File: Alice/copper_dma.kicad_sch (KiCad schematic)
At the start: 36 parts

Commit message: Copper DMA done
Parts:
- added AND_134, AND_136, AND_137, AND_138, AND_139, AND_140, AND_141, AND_142, AND_143, AND_39: AND2, symbol NMOS:AND2
- added AND_135: AND3, symbol NMOS:AND3
- added COP1_FF1, COP2_FF1, COP3_FF1: DFFR, symbol NMOS:DFFR
- added COP3D_FF1: DFFN, symbol NMOS:DFFN
- added NAND_9: NAND2, symbol NMOS:NAND2
- added NOR_34, NOR_35, NOR_37: NOR2, symbol NMOS:NOR2
- added NOR_36: NOR6, symbol NMOS:NOR6
- added NOR_38: NOR4, symbol NMOS:NOR4
- added NOT_36, NOT_37: NOT, symbol NMOS:NOT
- added OR_49, OR_51, OR_52: OR2, symbol NMOS:OR2
- added OR_50: OR4, symbol NMOS:OR4
- added Q898, Q899, Q900, Q901, Q902, Q903, Q904, Q905, Q906, Q907: NOT_OC, symbol NMOS:NOT_OC
- added SKIP_SR1: SR, symbol NMOS:SR
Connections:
- net COPEN: now also AND_128.3, AND_39.3; no longer AND_128.4
- net COPRES: now also COP1_FF1.6 (R), COP2_FF1.6 (R), COP3_FF1.6 (R), OR_52.2
- net COPSTART: now also AND_134.3, OR_49.3, OR_50.2
- net CPCE: now also AND_134.2, AND_137.3, AND_138.3, AND_139.3, AND_140.3, AND_141.3, AND_142.3
- net EQGT: now also AND_135.4, NOR_34.3
- net GND: now also NOR_36.3
- net HCTR1: now also AND_128.4, NOR_38.4, NOT_36.2; no longer AND_128.3
- net PHI1: now also COP1_FF1.4 (C1), COP2_FF1.4 (C1), COP3D_FF1.4 (C1), COP3_FF1.4 (C1), SKIP_SR1.4 (C1)
- net PHI2: now also AND_137.2, COP3D_FF1.5 (C2)
- net UCI1: now also AND_139.1, Q898.2, Q900.2, Q902.2, Q904.2, Q906.2
- net UCI2: now also AND_142.1, Q899.2, Q901.2, Q903.2, Q905.2, Q907.2
- net VALIDMOVE: now also AND_136.2, NOT_37.2
- net MOVE: now reaches AND_133.2, CIR1_LD0.2 (~{Q})
- net MOVE: now also NOR_36.4
- net CBR2: now reaches COPJMP_SR2.1 (Q), OR_47.2
- net CBR2: now also AND_141.2
- net at COPJMP_SR2.6 (R): now also COPJMP_SR1.6 (R), AND_134.1
- net CBR1: now reaches COPJMP_SR1.1 (Q), OR_47.3
- net CBR1: now also AND_140.2
- net SKIP_INS renamed SKIPINS
- net SKIPINS: now also AND_135.3, NOR_34.2
- new net: NOR_34.1, NOR_36.2
- new net: AND_39.2, NOT_36.1
- new net: COP2_FF1.3 (D), NOR_37.1
- new net: NOR_35.1, NOR_37.3
- new net: OR_52.1, SKIP_SR1.6 (R)
- new net: NOR_38.5, NOT_37.1
- new net: COP3D_FF1.2 (~{Q}), NAND_9.2
- new net: COP1_FF1.3 (D), OR_49.1
- new net: NAND_9.1, NOR_38.3
- new net CIPRQ: AND_139.2, OR_51.1
- new net COP1: AND_135.2, COP1_FF1.1 (Q), NOR_35.2, NOR_36.5, OR_50.5, OR_51.3
- new net COP2: AND_142.2, COP2_FF1.1 (Q), COP3_FF1.3 (D), NOR_36.6, NOR_37.2, OR_50.4
- new net COP3: AND_136.3, COP3D_FF1.3 (D), COP3_FF1.1 (Q), NAND_9.3, NOR_36.7, OR_52.3
- new net COPN1: NOR_36.1, OR_49.2
- new net COPRS: NOR_38.1
- new net CPCLK: AND_137.1, COP1_FF1.5 (C2), COP2_FF1.5 (C2), COP3_FF1.5 (C2), SKIP_SR1.5 (C2)
- new net CPRQ: AND_138.2, AND_143.2, OR_50.1
- new net DRB1: Q906.1, Q907.1
- new net DRB4: Q904.1, Q905.1
- new net DRB5: Q902.1, Q903.1
- new net DRB6: Q900.1, Q901.1
- new net DRB8: Q898.1, Q899.1
- new net ECPEN: AND_143.3, AND_39.1
- new net EUCP: AND_143.1
- new net SETSKIP: AND_135.1, SKIP_SR1.7 (S)
- new net SKIP: NOR_38.2, SKIP_SR1.1 (Q)
- new net UCB1: AND_140.1
- new net UCB2: AND_141.1
- new net UCP: AND_138.1
- new net VCOP3: AND_136.1, NOR_35.3, OR_50.3, OR_51.2
- no-connect marks 3 -> 4
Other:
- note added: "$08C"
- note added: "Copper Instruction register / Video Beam comparator"
- note added: "RGA generation : COPINS address"
- moved on the sheet: COPJMP_SR1, COPJMP_SR2, UCID_FF1, UCID_FF2, UCI_FF1, UCI_FF2

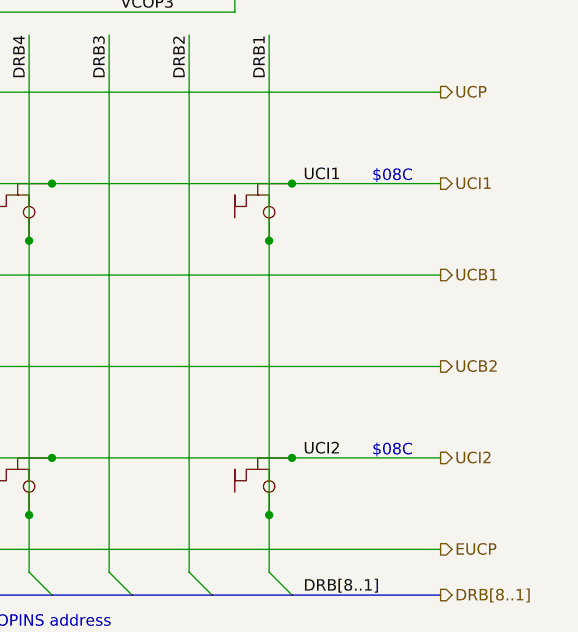
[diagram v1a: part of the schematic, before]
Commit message: Preparing DMA pointers sheet
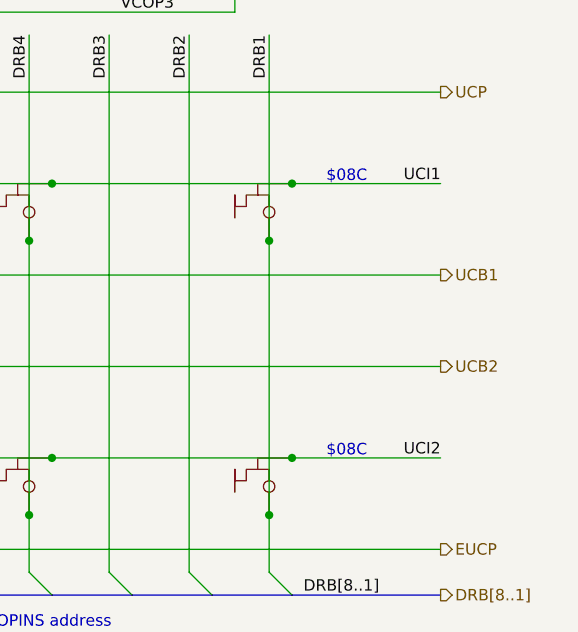
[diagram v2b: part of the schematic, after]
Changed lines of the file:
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@@
     (effects (font (size 1.27 1.27)) (justify left bottom))
   )
-  (text "$08C" (at 499.11 163.83 0)
-    (effects (font (size 1.27 1.27)) (justify left bottom))
-  )
-  (text "$08C" (at 499.11 133.35 0)
+  (text "$08C" (at 494.03 163.83 0)
+    (effects (font (size 1.27 1.27)) (justify left bottom))
+  )
+  (text "$08C" (at 494.03 133.35 0)
     (effects (font (size 1.27 1.27)) (justify left bottom))
   )
@@
     (effects (font (size 1.27 1.27)) (justify left bottom))
   )
-  (label "UCI1" (at 491.49 133.35 0)
-    (effects (font (size 1.27 1.27)) (justify left bottom))
+  (label "UCI1" (at 506.73 133.35 180)
+    (effects (font (size 1.27 1.27)) (justify right bottom))
   )
   (label "UCI2D" (at 280.67 201.93 0)
@@
     (effects (font (size 1.27 1.27)) (justify left bottom))
   )
-  (label "UCI2" (at 491.49 163.83 0)
-    (effects (font (size 1.27 1.27)) (justify left bottom))
+  (label "UCI2" (at 506.73 163.83 180)
+    (effects (font (size 1.27 1.27)) (justify right bottom))
   )
   (label "DRB4" (at 461.01 116.84 270)
@@
     (effects (font (size 1.27 1.27)) (justify right))
   )
-  (hierarchical_label "UCI2" (shape output) (at 506.73 163.83 0)
-    (effects (font (size 1.27 1.27)) (justify left))
-  )
   (hierarchical_label "UCP" (shape output) (at 506.73 123.19 0)
     (effects (font (size 1.27 1.27)) (justify left))
@@
     (effects (font (size 1.27 1.27)) (justify right))
   )
-  (hierarchical_label "UCI1" (shape output) (at 506.73 133.35 0)
-    (effects (font (size 1.27 1.27)) (justify left))
-  )
   (hierarchical_label "EUVP" (shape input) (at 254 163.83 180)
